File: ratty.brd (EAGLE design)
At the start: 616 x 652 mm, 95 parts, among them IC2 L293DD, Q1 BS170, Q2 BS170, Q3 BS170, Q5 BS170, U1 ITG-32001:1

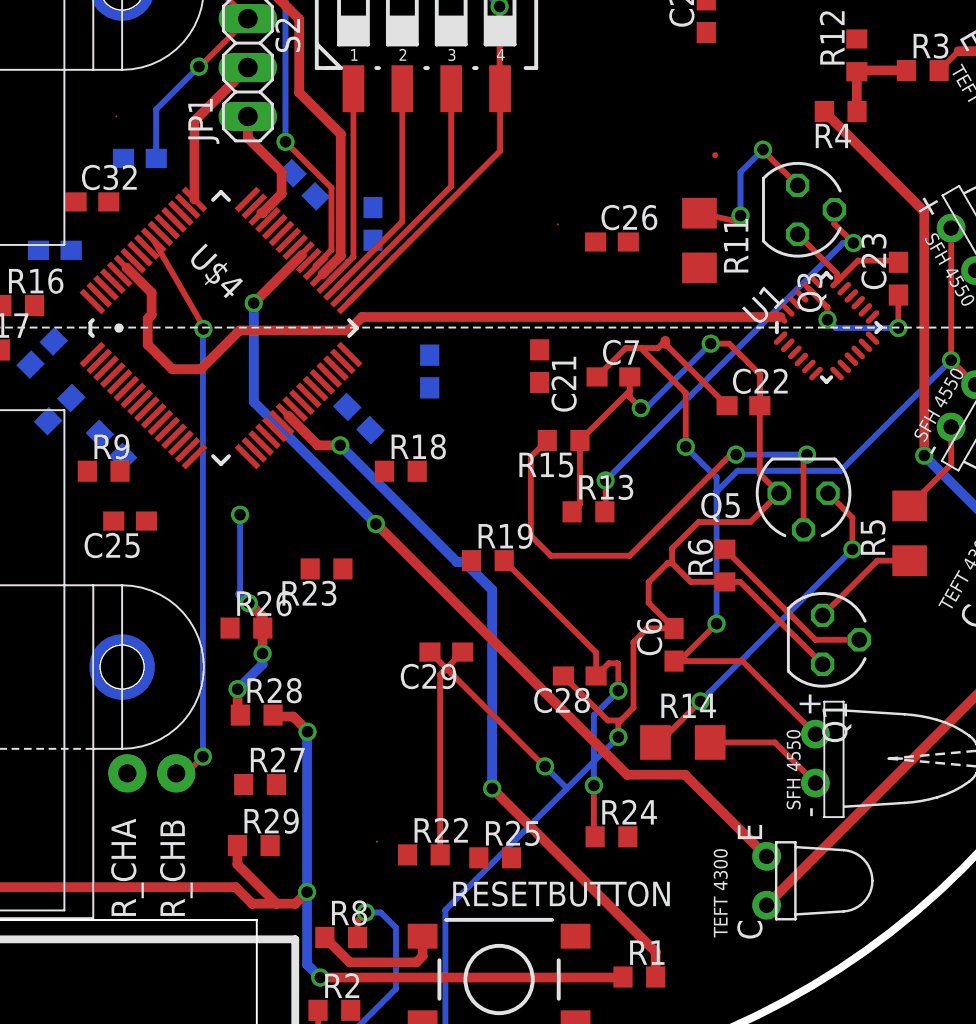
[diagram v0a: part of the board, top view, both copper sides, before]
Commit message: Fixed errors in schematics
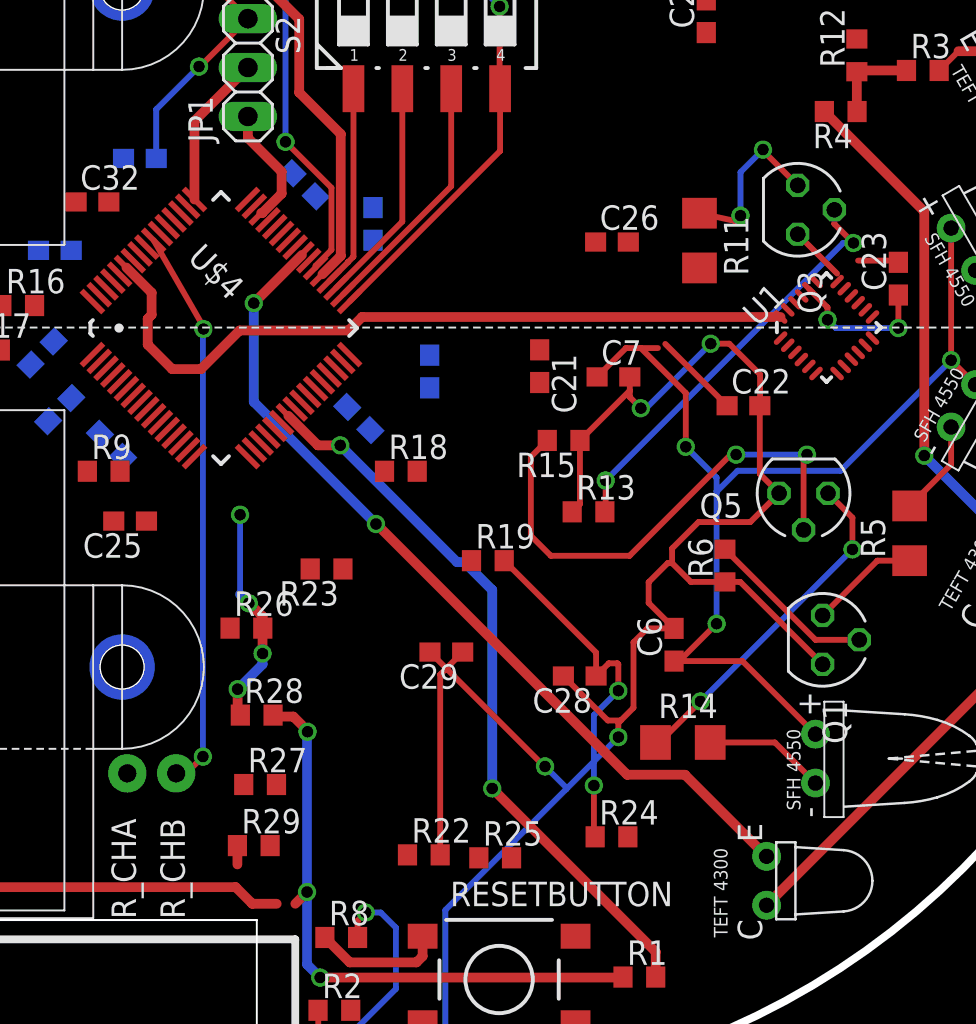
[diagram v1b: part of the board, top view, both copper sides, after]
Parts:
- removed SPLIT_GYRO_LOGIC, SPLIT_GYRO_VDD, SPLIT_VSS_CAP, U$22, U$7: SPLITTER, splitter:SPLITTER
- JP1: value (none) -> ConnectorPins
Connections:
- removed net GRYOREGOUT: U1.10
- removed net GRYOVLOGIC: U1.8
- removed net GYROVDD: C22.1, SPLIT_GYRO_VDD.1, U1.13
- removed net PA4_GYROLOGIC: SPLIT_GYRO_LOGIC.2, U$4.20
- removed net PIN30_VSS: C26.2, SPLIT_VSS_CAP.2
- removed net VDDA/VREF+: U$22.1
- removed net VSSA/VREF-: U$7.1
- net 3.3V: now also C22.1, U$17.A, U$4.13, U$4.19, U$4.32, U$4.48, U$4.64, U1.13; no longer U$22.2
- net 5V: no longer SPLIT_GYRO_VDD.2
- net AGND: now also U$4.12, U1.11, U1.12, U1.18, U1.9; no longer U$7.2
- net DGND: now also C26.2, D_SPLITTER.2, U$4.18, U$4.31, U$4.47, U$4.60, U$4.63; no longer SPLIT_VSS_CAP.1, U$17.A, U1.11, U1.18
- net GND: no longer D_SPLITTER.2, U1.12, U1.9
- net GYROREGOUT: now also U1.10
- net GYROVLOGIC: now also U$4.20, U1.8; no longer SPLIT_GYRO_LOGIC.1
- net PA_0_ENCODER1_1: now also U$4.14
- net PA_1_ENCODER1_2: now also U$4.15
- net PA_6_REC_CIRCUIT_2: now also U$4.22
- net PB_0_EMIT_CIRCUIT_3: now also U$4.26
- net PC_10_EMIT_CIRCUIT_1: now also U$4.51
- net PC_11_EMIT_CIRCUIT_2: now also U$4.52
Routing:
- net GYROVDD: track 4.71 -> 0.00 mm
- net 3.3V: track 37.5 -> 42.1 mm
- net AGND: track 41.4 -> 37.5 mm
- net DGND: track 199.9 -> 197.9 mm
- net 5V: track 187.3 -> 186.7 mm

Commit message: latest changes
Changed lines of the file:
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@@
 <wire x1="9.9568" y1="69.3166" x2="9.9568" y2="68.1618" width="0.508" layer="1"/>
 <wire x1="9.9568" y1="68.1618" x2="9.9178" y2="68.1228" width="0.508" layer="1"/>
-<wire x1="15.582" y1="50.3428" x2="9.9178" y2="68.1228" width="0" layer="19" extent="1-1"/>
 <wire x1="15.7852" y1="47.0408" x2="15.582" y2="50.3428" width="0" layer="19" extent="1-1"/>
 <wire x1="16.09" y1="43.9928" x2="15.7852" y2="47.0408" width="0" layer="19" extent="1-1"/>
@@
 <contactref element="U$4" pad="48"/>
 <contactref element="U$4" pad="64"/>
-<wire x1="43.442559375" y1="47.845040625" x2="48.3226" y2="76.7588" width="0" layer="19" extent="1-16"/>
+<wire x1="43.442559375" y1="47.845040625" x2="47.625" y2="44.362" width="0" layer="19" extent="16-16"/>
 <wire x1="41.10445625" y1="46.48395625" x2="43.442559375" y2="47.845040625" width="0" layer="19" extent="1-16"/>
-<wire x1="47.625" y1="44.362" x2="43.442559375" y2="47.845040625" width="0" layer="19" extent="16-16"/>
 <wire x1="46.40775625" y1="38.422940625" x2="47.625" y2="44.362" width="0" layer="19" extent="1-16"/>
+<wire x1="31.03024375" y1="39.107440625" x2="33.043440625" y2="38.422940625" width="0" layer="19" extent="1-16"/>
+<wire x1="31.94464375" y1="36.161040625" x2="33.043440625" y2="38.422940625" width="0" layer="19" extent="1-16"/>
 <wire x1="46.287359375" y1="35.703840625" x2="46.40775625" y2="38.422940625" width="0" layer="19" extent="1-16"/>
+<wire x1="30.2396" y1="43.8404" x2="32.1954" y2="46.355" width="0" layer="19" extent="1-16"/>
+<wire x1="34.6592" y1="48.6156" x2="32.1954" y2="46.355" width="0" layer="19" extent="1-16"/>
+<wire x1="34.63704375" y1="33.10475625" x2="31.94464375" y2="36.161040625" width="0" layer="19" extent="16-16"/>
+<wire x1="37.28608125" y1="34.1803" x2="34.63704375" y2="33.10475625" width="0" layer="19" extent="1-16"/>
 <wire x1="50.5714" y1="38.3912" x2="46.40775625" y2="38.422940625" width="0" layer="19" extent="1-16"/>
-<wire x1="41.8115625" y1="33.826746875" x2="46.287359375" y2="35.703840625" width="0" layer="19" extent="1-16"/>
-<wire x1="37.28608125" y1="34.1803" x2="41.8115625" y2="33.826746875" width="0" layer="19" extent="1-1"/>
-<wire x1="34.63704375" y1="33.10475625" x2="37.28608125" y2="34.1803" width="0" layer="19" extent="1-16"/>
-<wire x1="31.94464375" y1="36.161040625" x2="34.63704375" y2="33.10475625" width="0" layer="19" extent="16-16"/>
-<wire x1="33.043440625" y1="38.422940625" x2="31.94464375" y2="36.161040625" width="0" layer="19" extent="1-16"/>
-<wire x1="31.03024375" y1="39.107440625" x2="33.043440625" y2="38.422940625" width="0" layer="19" extent="1-16"/>
-<wire x1="33.043440625" y1="41.18065625" x2="33.043440625" y2="38.422940625" width="0" layer="19" extent="1-1"/>
-<wire x1="30.2396" y1="43.8404" x2="33.043440625" y2="41.18065625" width="0" layer="19" extent="1-16"/>
-<wire x1="32.1954" y1="46.355" x2="30.2396" y2="43.8404" width="0" layer="19" extent="1-16"/>
-<wire x1="34.6592" y1="48.6156" x2="32.1954" y2="46.355" width="0" layer="19" extent="1-16"/>
-<wire x1="24.2838" y1="40.578" x2="30.2396" y2="43.8404" width="0" layer="19" extent="1-16"/>
-<wire x1="44.362" y1="27.2796" x2="41.8115625" y2="33.826746875" width="0" layer="19" extent="1-1"/>
-<wire x1="62.8142" y1="38.9772" x2="50.5714" y2="38.3912" width="0" layer="19" extent="1-16"/>
+<wire x1="41.8115625" y1="33.826746875" x2="37.28608125" y2="34.1803" width="0" layer="19" extent="1-1"/>
 <wire x1="73.584096875" y1="40.3754875" x2="66.0282" y2="35.7632" width="0" layer="19" extent="1-1"/>
-<wire x1="54.825" y1="12.2682" x2="44.362" y2="27.2796" width="0" layer="19" extent="1-1"/>
-<wire x1="60.8702" y1="13.3604" x2="54.825" y2="12.2682" width="0" layer="19" extent="1-1"/>
-<wire x1="46.4684" y1="4.3434" x2="54.825" y2="12.2682" width="0" layer="19" extent="1-1"/>
-<wire x1="3.2512" y1="37.4142" x2="24.2838" y2="40.578" width="0" layer="19" extent="1-1"/>
+<wire x1="48.3226" y1="76.7588" x2="43.442559375" y2="47.845040625" width="0" layer="19" extent="1-16"/>
 </signal>
 <signal name="TO_C5_CAP">
@@
 <wire x1="35.9156" y1="40.2844" x2="36.1188" y2="40.4876" width="0.508" layer="1"/>
 <wire x1="36.1188" y1="40.4876" x2="36.1188" y2="41.64083125" width="0.508" layer="1"/>
-<wire x1="36.1188" y1="41.64083125" x2="34.81120625" y2="42.948425" width="0.508" layer="1"/>
+<wire x1="36.1188" y1="41.64083125" x2="34.81120625" y2="42.948425" width="0.3048" layer="1"/>
 </signal>
 <signal name="PB9_GYROCLK">
@@
 <wire x1="17.2974" y1="30.353" x2="17.2974" y2="31.6602" width="0.508" layer="1"/>
 <wire x1="17.2974" y1="31.6602" x2="17.2838" y2="31.6738" width="0.508" layer="1"/>
-<contactref element="C11" pad="2"/>
 <contactref element="C17" pad="2"/>
 <contactref element="C18" pad="2"/>
@@
 <contactref element="U$4" pad="63"/>
 <contactref element="U$4" pad="60"/>
+<contactref element="C11" pad="2"/>
 <wire x1="71.7444875" y1="42.6317125" x2="72.836390625" y2="43.307" width="0" layer="19" extent="1-1"/>
 <wire x1="67.7418" y1="37.3888" x2="71.7444875" y2="42.6317125" width="0" layer="19" extent="1-1"/>
@@
 <wire x1="41.1226" y1="49.6824" x2="42.8752" y2="47.9298" width="0.508" layer="1"/>
 <wire x1="42.8752" y1="47.9298" x2="42.8752" y2="46.7868" width="0.508" layer="1"/>
-<wire x1="42.8752" y1="46.7868" x2="41.86525" y2="45.77685" width="0.508" layer="1"/>
+<wire x1="42.8752" y1="46.7868" x2="41.86525" y2="45.77685" width="0.3048" layer="1"/>
 <wire x1="41.86525" y1="45.77685" x2="41.8115625" y2="45.77685" width="0.508" layer="1"/>
 </signal>
@@
 <wire x1="38.7858" y1="39.7256" x2="38.8112" y2="39.751" width="0.3048" layer="16"/>
 <via x="38.8112" y="39.751" extent="1-16" drill="0.6"/>
-<wire x1="38.8112" y1="39.751" x2="38.8112" y2="39.87185625" width="0.3048" layer="1"/>
-<wire x1="38.8112" y1="39.87185625" x2="36.22541875" y2="44.3626375" width="0.3048" layer="1"/>
+<wire x1="38.8112" y1="39.751" x2="38.8366" y2="41.77685625" width="0.3048" layer="1"/>
+<wire x1="38.8366" y1="41.77685625" x2="36.22541875" y2="44.3626375" width="0.3048" layer="1"/>
 </signal>
 <signal name="PA_7_REC_CIRCUIT_1">
@@
 <wire x1="41.4274" y1="35.9664" x2="41.4274" y2="41.0972" width="0.508" layer="16"/>
 <via x="41.4274" y="41.0972" extent="1-16" drill="0.6"/>
-<wire x1="41.4274" y1="41.0972" x2="43.932884375" y2="43.602684375" width="0.508" layer="1"/>
+<wire x1="41.4274" y1="41.0972" x2="43.932884375" y2="43.602684375" width="0.3048" layer="1"/>
 <wire x1="43.932884375" y1="43.602684375" x2="43.932884375" y2="43.65553125" width="0.3048" layer="1"/>
 <wire x1="43.932884375" y1="43.65553125" x2="72.771" y2="54.825" width="0" layer="19" extent="1-1"/>

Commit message: once again time to reroute
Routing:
- net 5V: track 186.7 -> 224.1 mm, vias 9 -> 11
- net DGND: track 197.9 -> 177.3 mm, vias 8 -> 6
- net 3.3V: track 42.1 -> 37.5 mm
- net PB7_I2CSDA_FOR_GYRO: track 39.2 -> 39.7 mm

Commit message: Routed 4 wires!!(not really)
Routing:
- net BATTERY_2: track 13.6 -> 104.6 mm, vias 0 -> 2
- net BATTERY: track 21.8 -> 78.4 mm, vias 0 -> 2
- net HBRIDGE_EN1: track 0.00 -> 51.3 mm, vias 0 -> 4
- net TO_C5_CAP: track 0.00 -> 46.7 mm, vias 0 -> 2
- net DIP_BUTTON_1: track 10.5 -> 55.7 mm, vias 0 -> 4
- net LEFT_FORWARD: track 0.00 -> 36.6 mm, vias 0 -> 2
- net DGND: track 177.3 -> 201.3 mm, vias 6 -> 10
- net RIGHT_FORWARD: track 22.9 -> 0.00 mm
- net 5V: track 224.1 -> 240.2 mm
- net GND: track 99.8 -> 106.9 mm, vias 3 -> 6
- net AGND: track 37.5 -> 41.4 mm
- net VOLTAGE_BATTERY_2: track 0.00 -> 3.75 mm
- net TO_R22/C29: track 11.0 -> 13.1 mm, vias 0 -> 2
- net PA_7_REC_CIRCUIT_1: track 38.0 -> 38.8 mm
- net TO_R19/C28: track 18.9 -> 18.4 mm
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
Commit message: More routing
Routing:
- net L_DIGITAL_IN_1: track 0.00 -> 60.5 mm, vias 0 -> 8
- net PA_1_ENCODER1_2: track 0.00 -> 55.2 mm, vias 0 -> 2
- net R_DIGITAL_IN_1: track 0.00 -> 51.9 mm, vias 0 -> 6
- net PA_0_ENCODER1_1: track 0.00 -> 47.1 mm, vias 0 -> 2
- net 5V: track 240.2 -> 276.2 mm, vias 11 -> 15
- net MGND: track 57.8 -> 90.4 mm, vias 3 -> 4
- net DGND: track 201.3 -> 223.3 mm, vias 10 -> 11
- net GND: track 106.9 -> 127.1 mm, vias 6 -> 8
- net N$18: track 0.00 -> 13.0 mm, vias 0 -> 2
- net N$20: track 0.00 -> 9.04 mm
- net BATTERY_2: track 104.6 -> 112.0 mm, vias 2 -> 6
- net 3.3V: track 37.5 -> 42.9 mm
- net LEFT_FORWARD: track 36.6 -> 40.4 mm

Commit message: attempted some more routes
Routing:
- net 3.3V: track 42.9 -> 5.36 mm, vias 2 -> 0
- net PA_5_ENCODER2_1: track 0.00 -> 26.1 mm, vias 0 -> 1
- net LEFT_BACK: track 0.00 -> 23.1 mm, vias 0 -> 2
- net BATTERY: track 78.4 -> 80.5 mm, vias 2 -> 3
- net HBRIDGE_EN1: track 51.3 -> 50.6 mm
- net BATTERY_2: track 112.0 -> 112.1 mm, vias 6 -> 8

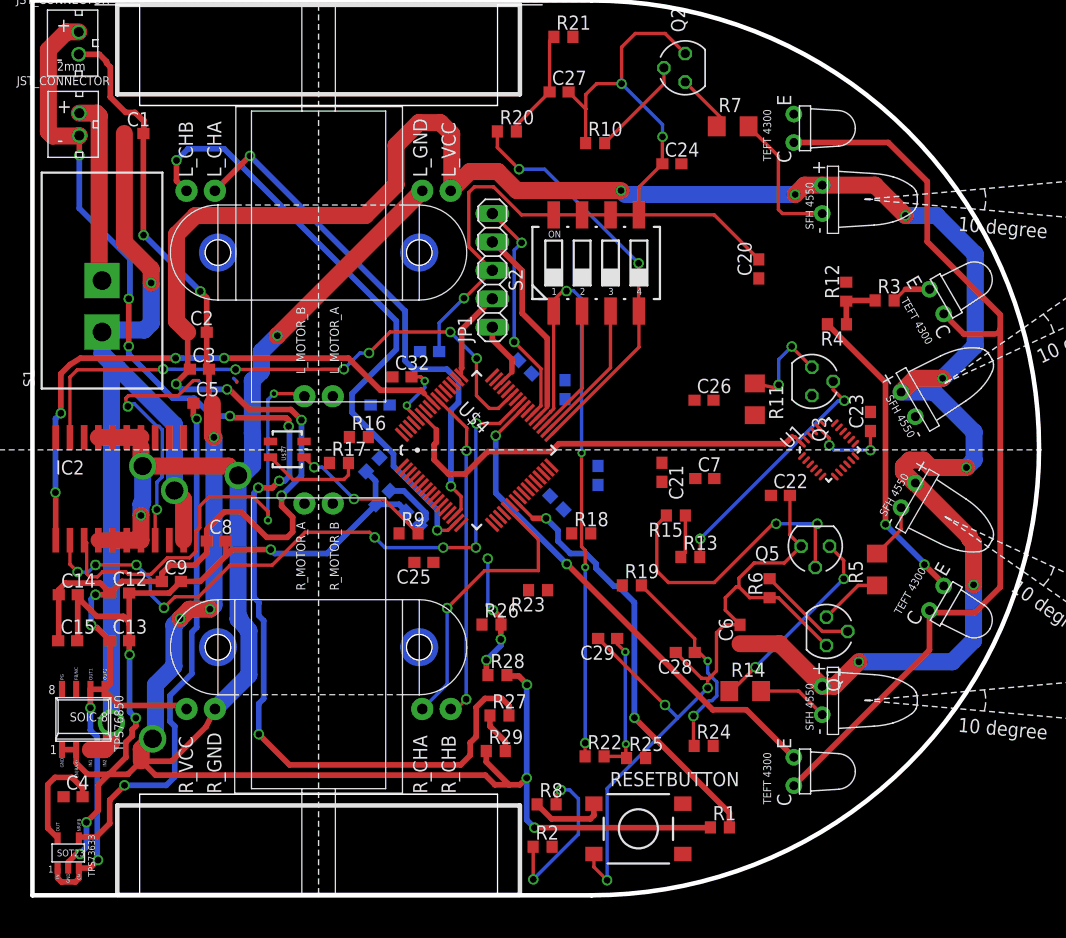
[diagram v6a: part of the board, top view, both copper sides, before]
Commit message: first autoroute with 14 airwires left
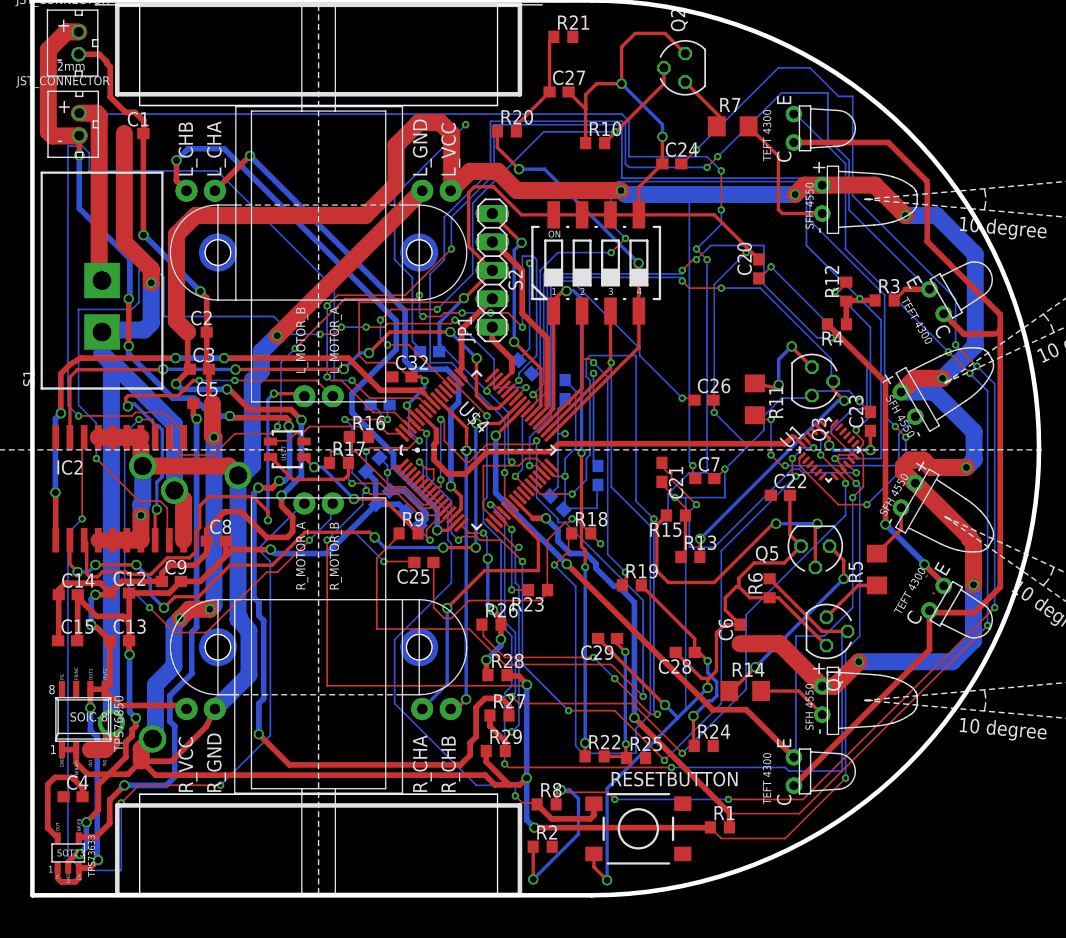
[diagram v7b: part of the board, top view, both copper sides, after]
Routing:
- net AGND: track 41.4 -> 223.0 mm, vias 3 -> 13
- net DGND: track 223.3 -> 380.1 mm, vias 11 -> 22
- net BATTERY_1: track 16.7 -> 150.6 mm, vias 0 -> 7
- net N$2: track 15.2 -> 132.4 mm, vias 2 -> 8
- net PB9_GYROCLK: track 0.00 -> 117.0 mm, vias 0 -> 6
- net PA_6_REC_CIRCUIT_2: track 3.58 -> 102.3 mm, vias 0 -> 3
- net GYROVLOGIC: track 0.00 -> 95.4 mm, vias 0 -> 6
- net RIGHT_FORWARD: track 0.00 -> 88.0 mm, vias 0 -> 3
- net HBRIDGE_EN2: track 0.00 -> 83.1 mm, vias 0 -> 2
- net PA_7_REC_CIRCUIT_1: track 38.8 -> 121.9 mm, vias 2 -> 5
- net RED_LED: track 0.00 -> 82.2 mm, vias 0 -> 4
- net PB8_I2C1SCL_FOR_GYRO: track 0.00 -> 80.2 mm, vias 0 -> 8
- net PC_10_EMIT_CIRCUIT_1: track 8.94 -> 88.8 mm, vias 0 -> 3
- net L_DIGITAL_IN_2: track 0.00 -> 78.7 mm, vias 0 -> 6
- net 3.3V: track 5.36 -> 81.0 mm, vias 0 -> 9
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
